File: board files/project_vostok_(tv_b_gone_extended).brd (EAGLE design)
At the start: 101 x 58 mm, 24 parts, among them IC1 ATMEGA644PV-10PU, IC2 MCP1825S-3302E_DB, Q5 MPS2907A, T1 2N3904, T2 2N3904, T3 2N3904, T4 2N3904, U1 PEC11R-4015F-S0024

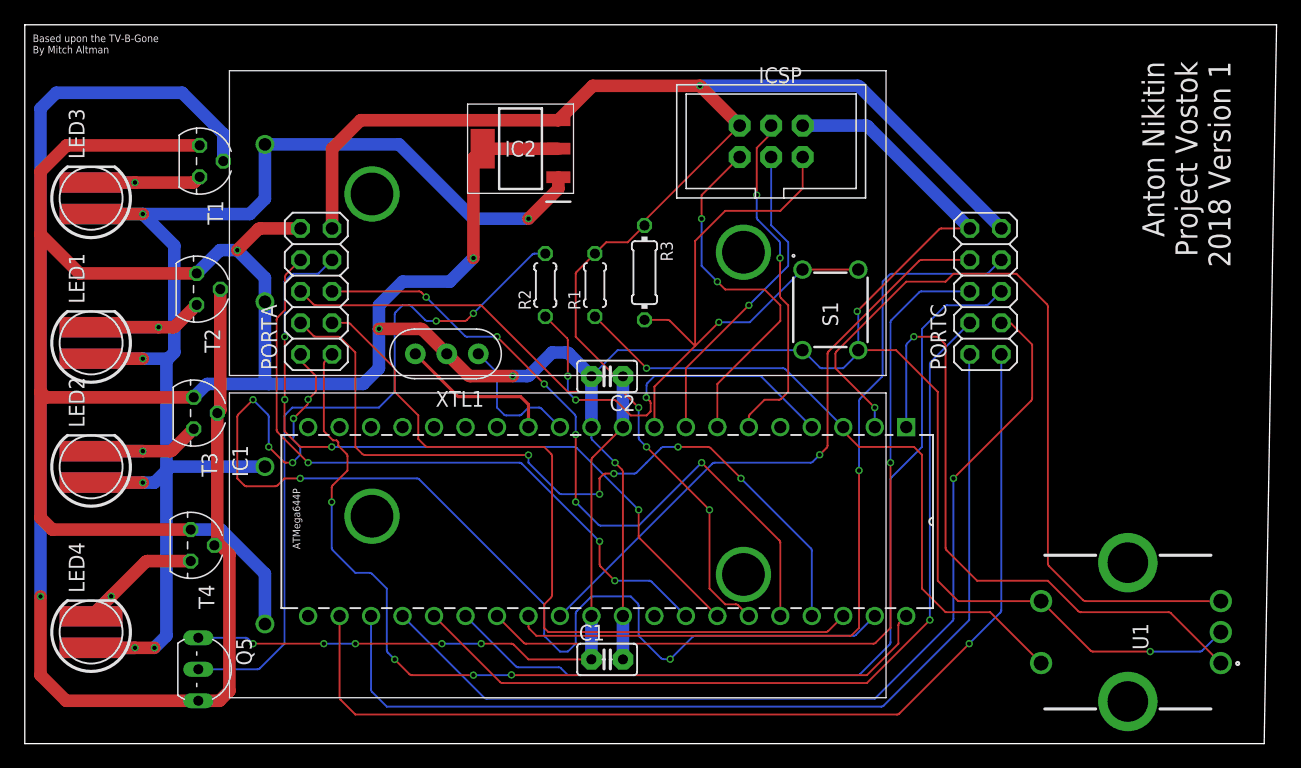
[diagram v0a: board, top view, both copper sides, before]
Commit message: removed wires and change battery orientation
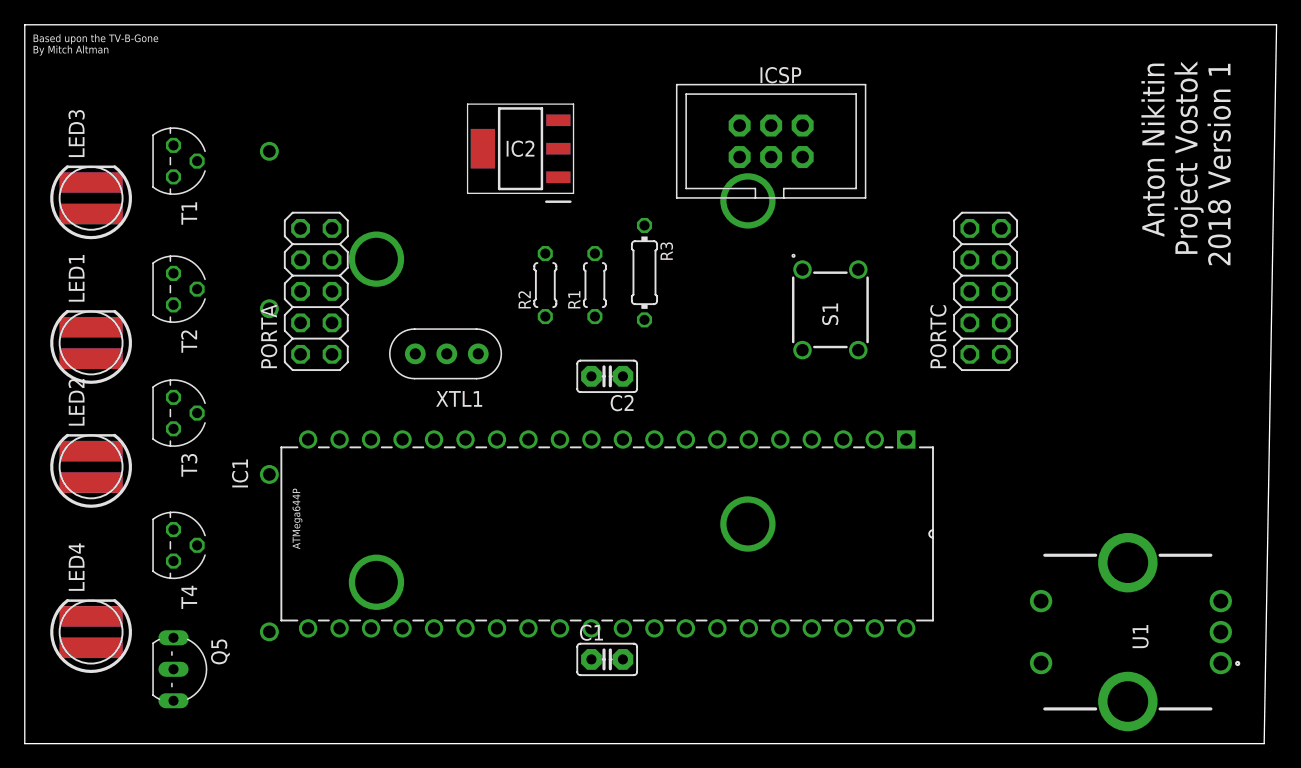
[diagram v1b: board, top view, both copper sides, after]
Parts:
- moved T1 2.11 mm to (12.0, 51.0)
- moved Q5 2.00 mm to (12.0, 10.0)
- moved T2 1.87 mm to (12.0, 40.7)
- moved T3 1.63 mm to (12.0, 30.7)
- moved T4 1.39 mm to (12.0, 20.0)
- moved IC1 1.00 mm to (22.9, 13.3)
- moved BAT_2 0.73 mm to (43.4, 19.4), flipped to the bottom, turned to 0 degrees
- moved BAT_1 0.67 mm to (43.4, 45.4), flipped to the bottom, turned to 0 degrees
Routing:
- net GND: track 307.9 -> 0.00 mm, vias 7 -> 0
- net VOUT_REG: track 156.7 -> 0.00 mm, vias 6 -> 0
- net VIN_REG: track 125.7 -> 0.00 mm, vias 6 -> 0
- net Q5_E: track 114.2 -> 0.00 mm, vias 1 -> 0
- net PA1: track 91.5 -> 0.00 mm, vias 7 -> 0
- net PC0: track 84.7 -> 0.00 mm, vias 1 -> 0
- net PC1: track 79.1 -> 0.00 mm
- net PC2: track 77.9 -> 0.00 mm, vias 1 -> 0
- net PA0: track 73.8 -> 0.00 mm, vias 4 -> 0
- net PC4: track 71.3 -> 0.00 mm
- net PC3: track 69.6 -> 0.00 mm, vias 1 -> 0
- net PC6: track 67.1 -> 0.00 mm, vias 1 -> 0
- net PC5: track 65.3 -> 0.00 mm, vias 1 -> 0
- net PB1: track 64.2 -> 0.00 mm, vias 1 -> 0
- net PA2: track 63.3 -> 0.00 mm
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
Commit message: modified routing
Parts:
- moved IC1 51.8 mm to (72.4, 28.6), turned to 90 degrees
- moved ICSP 37.0 mm to (91.3, 32.5), turned to 270 degrees
- moved XTL1 35.4 mm to (58.0, 9.37), turned to 0 degrees
- moved IC2 5.93 mm to (45.8, 53.3)
- moved C2 2.29 mm to (48.3, 31.7)
- moved C1 1.80 mm to (48.3, 9.53)
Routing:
- net GND: track 0.00 -> 271.7 mm, vias 0 -> 4
- net VOUT_REG: track 0.00 -> 193.6 mm, vias 0 -> 1
- net VIN_REG: track 0.00 -> 161.1 mm, vias 0 -> 6
- net PB1: track 0.00 -> 90.2 mm, vias 0 -> 1
- net RESET: track 0.00 -> 88.4 mm
- net PB2: track 0.00 -> 83.2 mm
- net PB0: track 0.00 -> 80.5 mm, vias 0 -> 2
- net MOSI: track 0.00 -> 70.7 mm, vias 0 -> 1
- net MISO: track 0.00 -> 60.4 mm, vias 0 -> 3
- net SCK: track 0.00 -> 60.0 mm, vias 0 -> 4
- net N$7: track 0.00 -> 56.0 mm, vias 0 -> 2
- net Q5_E: track 0.00 -> 47.0 mm
- net PC6: track 0.00 -> 31.6 mm
- net PC7: track 0.00 -> 31.6 mm
- net PB3: track 0.00 -> 29.3 mm
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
